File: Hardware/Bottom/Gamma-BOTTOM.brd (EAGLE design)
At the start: 0 parts

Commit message: Update to Top and Bottom Boards.  Top is not complete as of yet, and the bottom is ready for a check.  Routing not performed yet
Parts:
- added C1, C10, C11, C17, C18, C22: 100n, LinnesLab-Passives:C0603
- added C14, C19: 2.2n, LinnesLab-Passives:C0603
- added C15, C16: 2.2u, LinnesLab-Passives:C0603
- added C20: 22u, LinnesLab-Passives:C0603
- added C21: 22n, LinnesLab-Passives:C0603
- added IMU1: LSM6DS3_CAST, LinnesLab-Sensors:LSM6DS3_CAST
- added J1: (no value), LinnesLab-Connectors:1X07
- added OP3: (no value), LinnesLab-AnalogIC:SO14
- added OP4: (no value), LinnesLab-AnalogIC:SOT23-5
- added Q1: (no value), LinnesLab-DiscreteSemi:SOT23-3
- added R13, R15, R19, R21: 220k, LinnesLab-Passives:R0603
- added R14, R22: 10M, LinnesLab-Passives:R0603
- added R16: (no value), LinnesLab-Passives:R0603
- added R17, R18: 10k, LinnesLab-Passives:R0402
- added R20, R23: 1M, LinnesLab-Passives:R0603
- added R24: 10k, LinnesLab-Passives:R0603
- added U$3: (no value), LinnesLab-Connectors:PPG.MODULE.2
- added U$4: AD5171, LinnesLab-DigitalIC:SOT-23-8
- added U1: AD5242-SO16, LinnesLab-DigitalIC:SO16
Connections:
- new net 3.3V: C1.2, C11.2, C17.2, C18.2, C22.2, IMU1.2, OP3.4, OP4.5, R13.2, R15.2, R17.2, U$3.V+, U$4.2, U$4.6, U1.5, U1.6
- new net A6/TIA: C10.2, C15.1, J1.5, OP4.1, U1.3
- new net A7/PPG: C21.2, J1.7, OP3.1, U1.14
- new net D29/LED.CTRL: J1.6, U$4.8
- new net G.A1: U1.2
- new net G.A2: U1.16
- new net G.O1: U1.1
- new net G.O2: U1.13
- new net G.W2: C21.1, OP3.2, R24.1, U1.15
- new net GND: C1.1, C11.1, C17.1, C18.1, C22.1, IMU1.1, OP3.11, OP4.2, OP4.3, Q1.2, R18.1, R19.1, R21.1, U$3.GND, U$4.3, U1.10, U1.11, U1.12, U1.9
- new net LED: Q1.3
- new net LED.C: U$3.LD1
- new net N$10: OP3.12, R17.1, R18.2
- new net N$13: C15.2, OP3.5, R13.1, R19.2
- new net N$15: C14.2, OP3.6, R14.1, R20.2
- new net N$16: C14.1, C16.1, OP3.7, R14.2
- new net N$17: C16.2, OP3.10, R15.1, R21.2
- new net N$18: C19.2, OP3.9, R22.1, R23.2
- new net N$19: C19.1, C20.1, OP3.8, R22.2
- new net N$20: C20.2, R24.2
- new net N$8: Q1.1, R16.2
- new net N$9: R16.1, U$4.1, U$4.7
- new net PD.C: C10.1, OP4.4, U$3.PD, U1.4
- new net SCL: IMU1.3, U$4.4, U1.7
- new net SDA: IMU1.4, U$4.5, U1.8
- new net VREF: OP3.13, OP3.14, OP3.3, R20.1, R23.1
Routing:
- added copper zone on layer 1, net 3.3V
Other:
- board outline added: 33 x 33 mm

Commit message: Finished Bottom Board as of Take 003
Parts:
- removed J1: (no value), LinnesLab-Connectors:1X07
- removed OP4: (no value), LinnesLab-AnalogIC:SOT23-5
- removed U$4: AD5171, LinnesLab-DigitalIC:SOT-23-8
- removed U1: AD5242-SO16, LinnesLab-DigitalIC:SO16
- added AD5171: AD5171, LinnesLab-DigitalIC:SOT-23-8
- added AD5242: AD5242-SO16, LinnesLab-DigitalIC:SO16
- added C2: 100n, LinnesLab-Passives:C0603
- added J2: (no value), LinnesLab-Connectors:1X07_1.27MM
- added TIA: (no value), LinnesLab-AnalogIC:SOT23-5
- moved R13 33.6 mm to (33.7, 5.44), turned to 270 degrees
- moved C14 29.0 mm to (29.6, 8.25), turned to 180 degrees
- moved R19 28.6 mm to (33.7, 9.12), turned to 270 degrees
- moved C15 27.3 mm to (30.0, 4.29), turned to 0 degrees
- moved R14 26.2 mm to (29.5, 9.67), turned to 0 degrees
- moved R16 23.2 mm to (19.1, 29.1)
- moved C11 23.1 mm to (25.6, 8.29), turned to 90 degrees
- moved IMU1 22.9 mm to (6.50, 28.1), turned to 90 degrees
- moved C20 22.5 mm to (21.5, 6.75), turned to 270 degrees
- moved R20 22.1 mm to (29.8, 6.55), turned to 180 degrees
- moved C16 20.7 mm to (33.8, 15.0), turned to 90 degrees
- moved R17 20.3 mm to (24.8, 19.6), turned to 90 degrees
- moved R18 18.5 mm to (23.3, 19.7), turned to 270 degrees
- moved C1 17.9 mm to (6.15, 23.7), turned to 0 degrees
- moved Q1 17.3 mm to (19.0, 26.5), turned to 180 degrees
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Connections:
- removed net LED: Q1.3
- net 3.3V: now also AD5171.2, AD5171.6, AD5242.5, AD5242.6, J2.4, TIA.5; no longer OP4.5, U$4.2, U$4.6, U1.5, U1.6
- net A6/TIA: now also AD5242.3, J2.6, TIA.1; no longer J1.5, OP4.1, U1.3
- net A7/PPG: now also AD5242.14, J2.7; no longer J1.7, U1.14
- net D29/LED.CTRL: now also AD5171.8, J2.5; no longer J1.6, U$4.8
- net G.A1: now also AD5242.2; no longer U1.2
- net G.A2: now also AD5242.16; no longer U1.16
- net G.O1: now also AD5242.1; no longer U1.1
- net G.O2: now also AD5242.13; no longer U1.13
- net G.W2: now also AD5242.15; no longer U1.15
- net GND: now also AD5171.3, AD5242.10, AD5242.11, AD5242.12, AD5242.9, C2.1, J2.3, TIA.2, TIA.3; no longer OP4.2, OP4.3, U$4.3, U1.10, U1.11, U1.12, U1.9
- net LED.C: now also Q1.3
- net N$9: now also AD5171.1, AD5171.7; no longer U$4.1, U$4.7
- net PD.C: now also AD5242.4, TIA.4; no longer OP4.4, U1.4
- net SCL: now also AD5171.4, AD5242.7, J2.2; no longer U$4.4, U1.7
- net SDA: now also AD5171.5, AD5242.8, J2.1; no longer U$4.5, U1.8
- net VREF: now also C2.2
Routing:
- net A6/TIA: track 0.00 -> 62.9 mm, vias 0 -> 4
- net A7/PPG: track 0.00 -> 49.1 mm
- net SDA: track 0.00 -> 38.7 mm
- net SCL: track 0.00 -> 37.9 mm, vias 0 -> 2
- net VREF: track 0.00 -> 33.7 mm, vias 0 -> 3
- net GND: track 0.00 -> 27.2 mm, vias 0 -> 15
- net PD.C: track 0.00 -> 24.7 mm, vias 0 -> 2
- net N$19: track 0.00 -> 21.1 mm
- net N$9: track 0.00 -> 20.0 mm
- net G.W2: track 0.00 -> 18.1 mm, vias 0 -> 2
- net D29/LED.CTRL: track 0.00 -> 16.7 mm, vias 0 -> 2
- net N$13: track 0.00 -> 16.1 mm
- net N$17: track 0.00 -> 10.2 mm, vias 0 -> 2
- net N$16: track 0.00 -> 9.94 mm
- net N$18: track 0.00 -> 6.45 mm
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- added copper zone on layer 16, net GND

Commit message: Pushed Changes to where I'm at (Take 007)
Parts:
- added C12, C3, C5: 1u, LinnesLab-Passives:C0603
- added C13, C4: 4.7u, LinnesLab-Passives:C0603
- added CHRG1: MCP73831, LinnesLab-Power:SOT23-5
- added LDO1: MIC5504, LinnesLab-Power:SOT23-5
- added R3: 100k, LinnesLab-Passives:R0603
- added R8: (no value), LinnesLab-Passives:R0603
- added U4: PCF8523, LinnesLab-Clocks:SO8
- added XTAL2: 32.7680kHz, LinnesLab-Clocks:2-SMD.NOLEAD.2.0MMTO1.2MM
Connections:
- new net D27/CHRG.STATUS: CHRG1.1, R3.1
- new net N$1: U4.2, XTAL2.P$1
- new net N$2: U4.1, XTAL2.P$2
- new net N$3: CHRG1.5, R8.2
- new net VBATT: U4.3
- new net VIN1: C4.2, C5.2, CHRG1.4, LDO1.1, LDO1.3, R3.2
- new net VLIPO: C13.1, CHRG1.3
- net 3.3V: now also C12.1, C3.1, LDO1.5, U4.8
- net GND: now also C12.2, C13.2, C3.2, C4.1, C5.1, CHRG1.2, LDO1.2, R8.1, U4.4
- net SCL: now also U4.6
- net SDA: now also U4.5

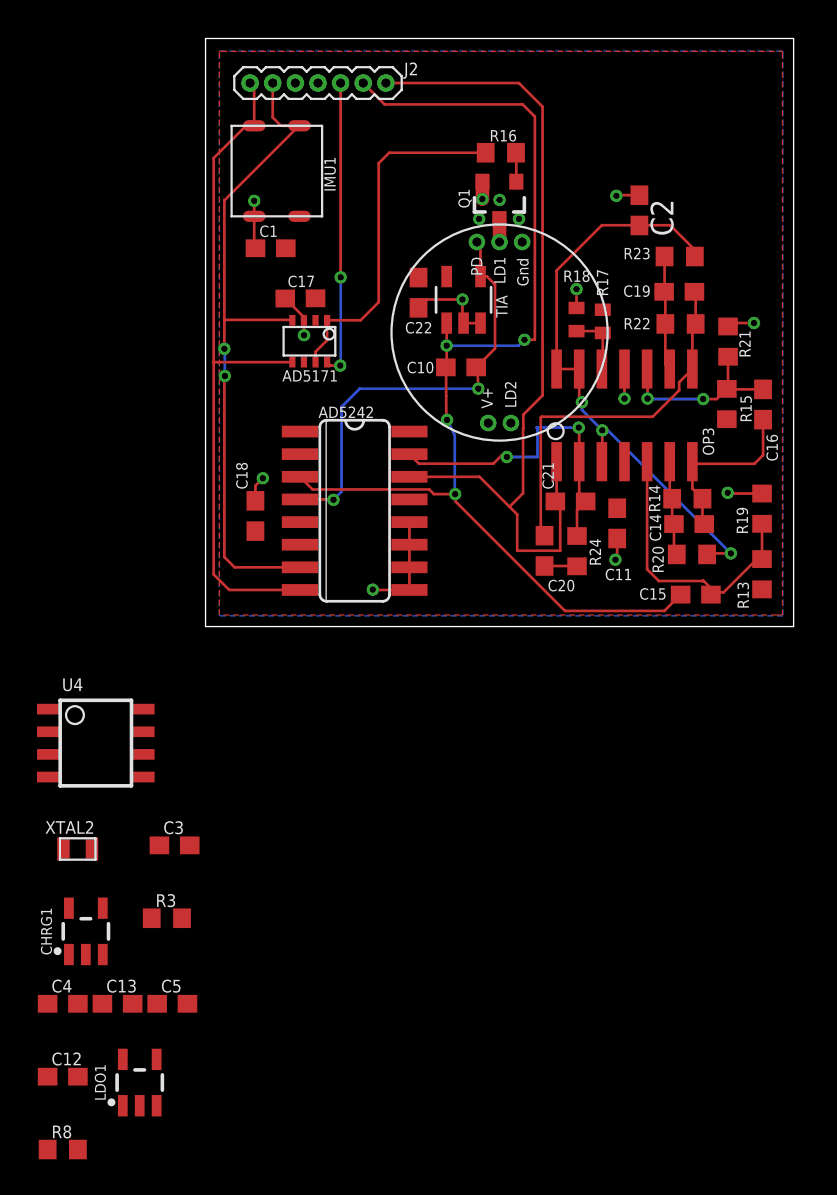
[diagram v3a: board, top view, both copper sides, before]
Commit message: Finished with Preliminary Version A of Smartwatch as of end of Take 008 video
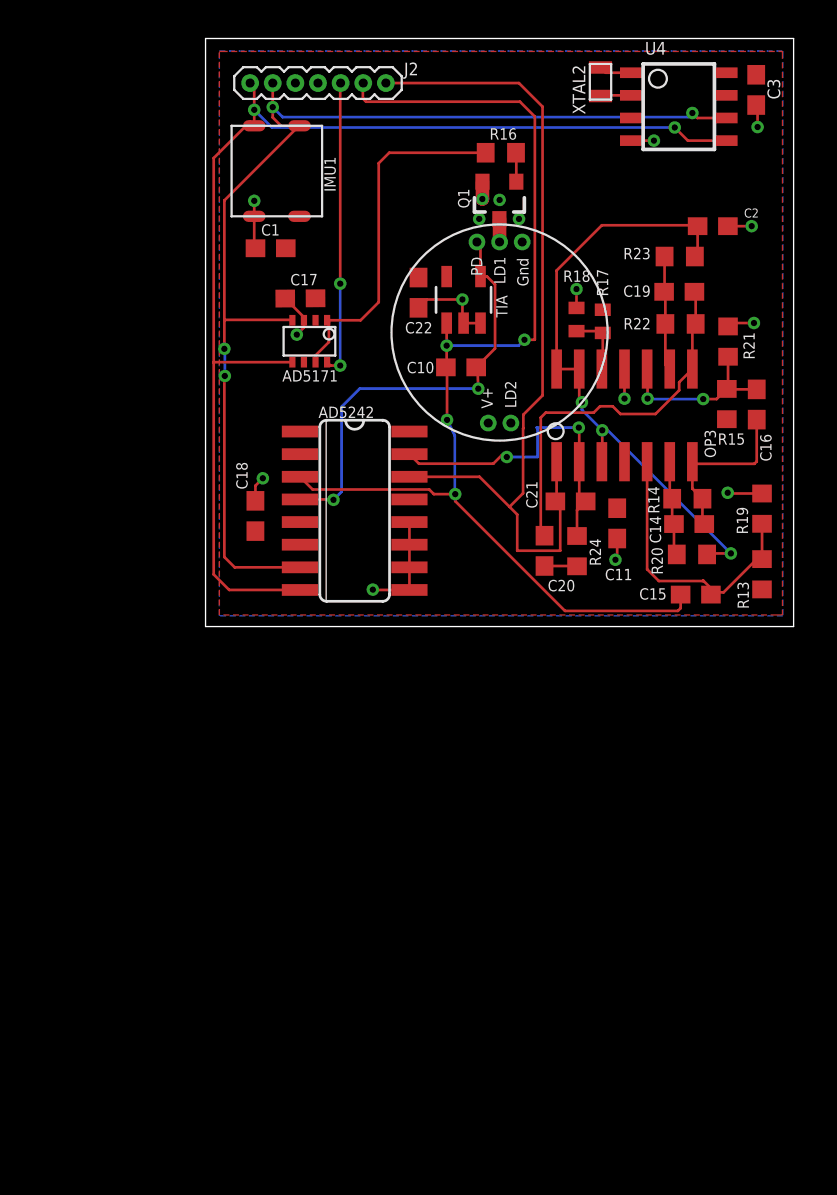
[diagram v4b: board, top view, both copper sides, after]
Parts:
- removed C12, C5: 1u, LinnesLab-Passives:C0603
- removed C13, C4: 4.7u, LinnesLab-Passives:C0603
- removed CHRG1: MCP73831, LinnesLab-Power:SOT23-5
- removed LDO1: MIC5504, LinnesLab-Power:SOT23-5
- removed R3: 100k, LinnesLab-Passives:R0603
- removed R8: (no value), LinnesLab-Passives:R0603
- moved C3 53.5 mm to (33.4, 32.6), turned to 270 degrees
- moved XTAL2 52.1 mm to (24.7, 33.1), turned to 90 degrees
- moved U4 48.4 mm to (29.1, 31.7)
- moved C2 4.21 mm to (31.0, 25.0), turned to 180 degrees
- moved C16 0.36 mm to (33.4, 15.0)
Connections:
- net A6/TIA renamed A5/TIA
- net A7/PPG renamed A4/PPG
- net D29/LED.CTRL renamed D30/LED.CTRL
- removed net D27/CHRG.STATUS: CHRG1.1, R3.1
- removed net N$3: CHRG1.5, R8.2
- removed net VIN1: C4.2, C5.2, CHRG1.4, LDO1.1, LDO1.3, R3.2
- removed net VLIPO: C13.1, CHRG1.3
- net 3.3V: no longer C12.1, LDO1.5
- net GND: no longer C12.2, C13.2, C4.1, C5.1, CHRG1.2, LDO1.2, R8.1
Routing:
- net SDA: track 38.7 -> 65.9 mm, vias 0 -> 2
- net SCL: track 37.9 -> 63.8 mm, vias 2 -> 4
- net GND: track 27.2 -> 29.8 mm, vias 15 -> 17
- net N$2: track 0.00 -> 1.87 mm
- net N$1: track 0.00 -> 1.76 mm
- net A5/TIA: track 62.9 -> 63.8 mm
- net VREF: track 33.7 -> 34.7 mm

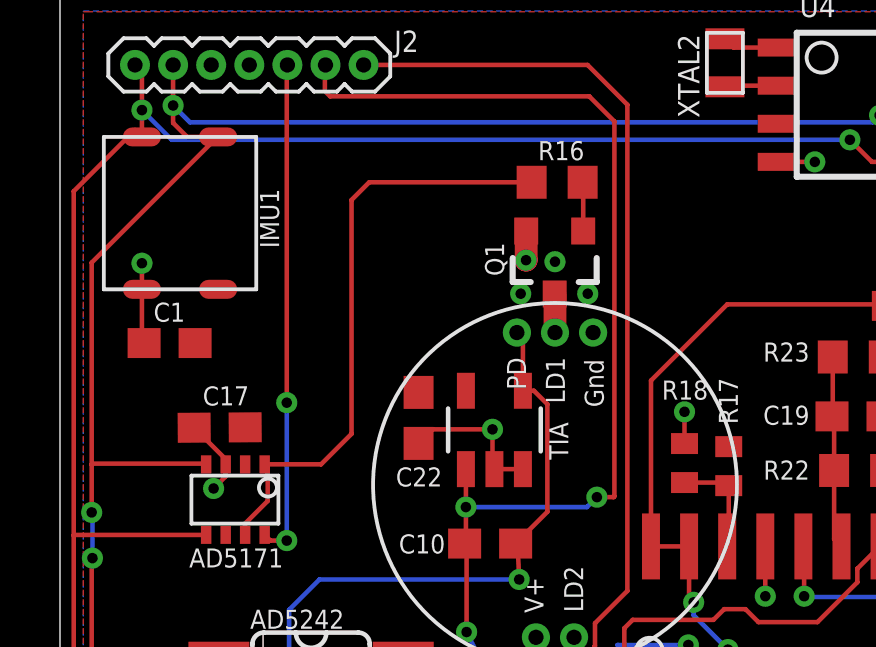
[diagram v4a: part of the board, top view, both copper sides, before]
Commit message: Updated file names and completed preliminary BOM for each board
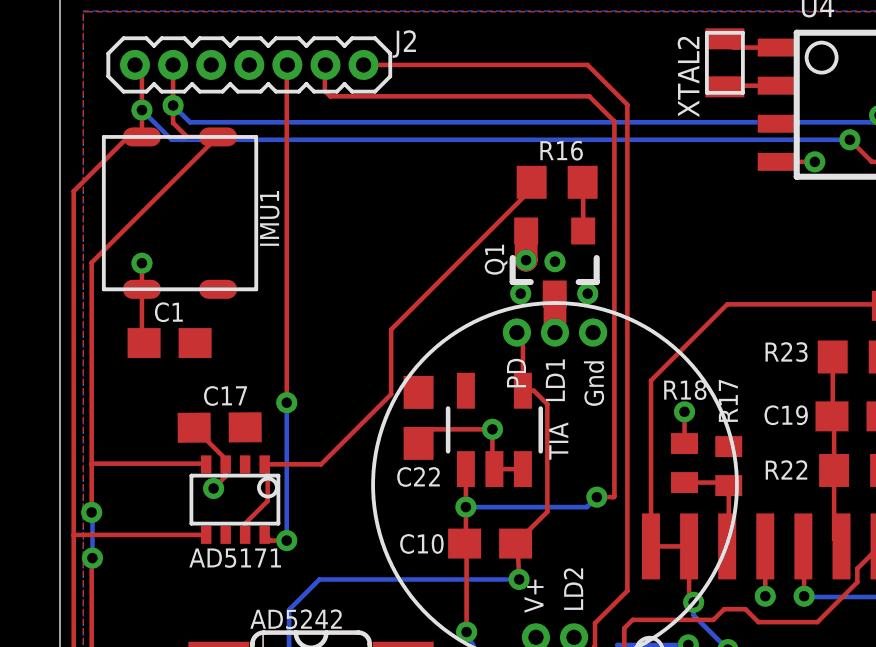
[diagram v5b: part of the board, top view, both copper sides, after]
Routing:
- net N$9: track 20.1 -> 16.9 mm
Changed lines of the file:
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@@
 <contactref element="AD5171" pad="1"/>
 <contactref element="R16" pad="1"/>
-<wire x1="12.2174" y1="20.702315625" x2="11.202484375" y2="19.6874" width="0.1524" layer="1"/>
+<wire x1="13.5382" y1="22.023115625" x2="11.202484375" y2="19.6874" width="0.1524" layer="1"/>
 <wire x1="9.3218" y1="19.6874" x2="11.202484375" y2="19.6874" width="0.1524" layer="1"/>
-<wire x1="12.2174" y1="20.702315625" x2="12.2174" y2="28.4988" width="0.1524" layer="1"/>
-<wire x1="12.2174" y1="28.4988" x2="12.8072" y2="29.0886" width="0.1524" layer="1"/>
-<wire x1="12.8072" y1="29.0886" x2="18.2216" y2="29.0886" width="0.1524" layer="1"/>
+<wire x1="13.5382" y1="24.1808" x2="13.5382" y2="22.023115625" width="0.1524" layer="1"/>
+<wire x1="18.2216" y1="29.0886" x2="18.2216" y2="28.8642" width="0.1524" layer="1"/>
+<wire x1="18.2216" y1="28.8642" x2="13.5382" y2="24.1808" width="0.1524" layer="1"/>
 <wire x1="8.6718" y1="17.3346" x2="8.6718" y2="17.7142" width="0.1524" layer="1"/>
 <wire x1="8.6718" y1="17.7142" x2="9.4234" y2="18.4658" width="0.1524" layer="1"/>

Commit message: small fixes
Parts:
- moved R16 0.48 mm to (19.1, 29.6)
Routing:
- net N$9: track 16.9 -> 18.3 mm
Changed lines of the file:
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@@
 <?xml version="1.0" encoding="utf-8"?>
 <!DOCTYPE eagle SYSTEM "eagle.dtd">
-<eagle version="9.5.2">
+<eagle version="9.6.2">
 <drawing>
 <settings>
@@
 <attribute name="VALUE" x="29.8488" y="15.621" size="1.27" layer="27" rot="R270"/>
 </element>
-<element name="R16" library="LinnesLab-Passives" package="R0603" package3d_urn="urn:adsk.eagle:package:15661944/2" value="" x="19.0716" y="29.0886" smashed="yes">
-<attribute name="NAME" x="18.4366" y="29.8252" size="0.635" layer="25"/>
-<attribute name="VALUE" x="18.4366" y="27.1836" size="1.27" layer="27"/>
+<element name="R16" library="LinnesLab-Passives" package="R0603" package3d_urn="urn:adsk.eagle:package:15661944/2" value="" x="19.0716" y="29.5712" smashed="yes">
+<attribute name="NAME" x="18.4366" y="30.3078" size="0.635" layer="25"/>
+<attribute name="VALUE" x="18.4366" y="27.6662" size="1.27" layer="27"/>
 </element>
 <element name="OP3" library="LinnesLab-AnalogIC" package="SO14" package3d_urn="urn:adsk.eagle:package:17879189/2" value="" x="26.0096" y="14.351" smashed="yes">
@@
 <contactref element="R16" pad="2"/>
 <contactref element="Q1" pad="1"/>
-<wire x1="19.9398" y1="27.464" x2="19.9398" y2="29.0704" width="0.1524" layer="1"/>
-<wire x1="19.9398" y1="29.0704" x2="19.9216" y2="29.0886" width="0.1524" layer="1"/>
+<wire x1="19.9398" y1="27.464" x2="19.9398" y2="29.553" width="0.1524" layer="1"/>
+<wire x1="19.9398" y1="29.553" x2="19.9216" y2="29.5712" width="0.1524" layer="1"/>
 </signal>
 <signal name="VREF">
@@
 <contactref element="AD5171" pad="1"/>
 <contactref element="R16" pad="1"/>
-<wire x1="13.5382" y1="22.023115625" x2="11.202484375" y2="19.6874" width="0.1524" layer="1"/>
+<wire x1="12.2428" y1="20.727715625" x2="11.202484375" y2="19.6874" width="0.1524" layer="1"/>
 <wire x1="9.3218" y1="19.6874" x2="11.202484375" y2="19.6874" width="0.1524" layer="1"/>
-<wire x1="13.5382" y1="24.1808" x2="13.5382" y2="22.023115625" width="0.1524" layer="1"/>
-<wire x1="18.2216" y1="29.0886" x2="18.2216" y2="28.8642" width="0.1524" layer="1"/>
-<wire x1="18.2216" y1="28.8642" x2="13.5382" y2="24.1808" width="0.1524" layer="1"/>
+<wire x1="12.2428" y1="25.2476" x2="12.2428" y2="20.727715625" width="0.1524" layer="1"/>
+<wire x1="18.2216" y1="29.5712" x2="16.5664" y2="29.5712" width="0.1524" layer="1"/>
+<wire x1="16.5664" y1="29.5712" x2="12.2428" y2="25.2476" width="0.1524" layer="1"/>
 <wire x1="8.6718" y1="17.3346" x2="8.6718" y2="17.7142" width="0.1524" layer="1"/>
 <wire x1="8.6718" y1="17.7142" x2="9.4234" y2="18.4658" width="0.1524" layer="1"/>
@@
 <wire x1="10.0584" y1="17.145" x2="9.5114" y2="17.145" width="0.1524" layer="1"/>
 <wire x1="9.5114" y1="17.145" x2="9.3218" y2="17.3346" width="0.1524" layer="1"/>
-<wire x1="10.0584" y1="17.145" x2="10.0584" y2="21.7424" width="0.1524" layer="16"/>
-<via x="10.0584" y="21.7424" extent="1-16" drill="0.35"/>
-<wire x1="10.0584" y1="21.7424" x2="10.0584" y2="32.9784" width="0.1524" layer="1"/>
-<wire x1="10.0584" y1="32.9784" x2="10.08" y2="33" width="0.1524" layer="1"/>
+<wire x1="10.0584" y1="17.145" x2="10.1092" y2="17.1958" width="0.1524" layer="16"/>
+<wire x1="10.1092" y1="22.9108" x2="10.1092" y2="17.1958" width="0.1524" layer="16"/>
+<via x="10.1092" y="22.9108" extent="1-16" drill="0.35"/>
+<wire x1="10.08" y1="33" x2="10.1092" y2="32.9708" width="0.1524" layer="1"/>
+<wire x1="10.1092" y1="32.9708" x2="10.1092" y2="22.9108" width="0.1524" layer="1"/>
 </signal>
 </signals>
